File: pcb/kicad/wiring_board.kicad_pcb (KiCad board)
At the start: 2 copper layers, 47 x 72 mm, 13 parts, among them J1 2604-1106, J2 5V out (flex jumper)

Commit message: Boards for v0.4: ring board, mic carrier, riser, cover flex, EU cap board, wiring board posts
- Ring board, mic carrier and riser in pcb/sensor/ (D-50, D-60, D-68); carrier and riser fab
  packs; the ring board waits on the MSR-2's CN2 part and map
- Riser 14 x 12 mm, pins above and between the posts; cover flex with the run past the GND
  contact post and a jog from the pad section (D-79)
- EU cap board on the carrier, closed snap windows, wider with the face plate (D-56, D-70,
  D-77, D-78); EU 5 V board pins follow the back cover's pads
- Wiring board: WA-SMSI spacer posts in the 5 V area (SMT, spigot inside the board), J2
- ERC / DRC clean on every board
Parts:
- removed C1: 22uF 10V X5R, wiring_board:C_1206_3216Metric
- added P1: +5V post, wiring_board:Wurth_WA-SMSI_M2_SMT_Spacer_L7mm, F.Cu at (109.8, 116.5)
- added P2: GND post, wiring_board:Wurth_WA-SMSI_M2_SMT_Spacer_L7mm, F.Cu at (116.7, 116.5)
- J2: value 5V out (flex jumper) -> 5V out (FFC to the ring board)
- MH1, MH2, MH3, MH4: value MountingHole_2.6mm_NPTH -> MountingHole_3.2mm_M3_NPTH; footprint wiring_board:MountingHole_2.6mm_NPTH -> wiring_board:MountingHole_3.2mm_M3_NPTH
- moved J2 5.32 mm to (113.5, 124.8), turned to 90 degrees
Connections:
- J2 pad 2: GND -> +5V
- J2 pad 4: +5V -> GND
- J2 pad 6: +5V -> GND
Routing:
- net GND: track 15.1 -> 22.9 mm
- net +5V: track 15.6 -> 20.1 mm, vias 0 -> 2
- net /PE: vias 48 -> 46
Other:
- board text added: "2026-10-11"
- board text added: "P1 Wurth WA-SMSI M2 L7"
- board text added: "P2 Wurth WA-SMSI M2 L7"
- board text added: "wiring_board v0.4"
- board text removed: "2026-10-09"
- board text removed: "C1 22uF 10V X5R 1206"
- board text removed: "wiring_board v0.3"

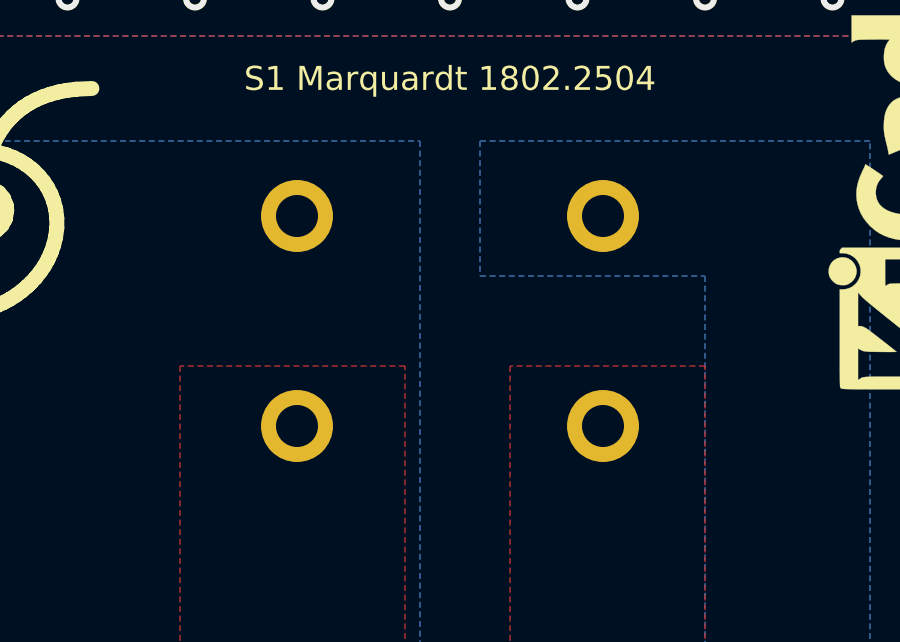
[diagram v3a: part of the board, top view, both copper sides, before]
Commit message: Mic on the boards, parts audit, rocker second source, CN2 land pattern, back cover fit (D-82..D-90)
- Prototype PCBWay packs for the ring board, EU cap board and cover flex; logos and URL on the
  boards with room for them
- CN2 mate: Molex 55909-2474 on an assumed 51338-2474 (D-82); land pattern from Molex
  SD-55909-003 rev J, B2B from SD-51338-003 rev K (D-89); contact map and pin 1 still open
- Microphone: Knowles SPK0641HT4H-1 + ADAU7002 on the ring board and the EU cap board, the mic
  carrier removed; face plate sound column on a gasket (D-83); C3 KEMET C1206C104J3GACTU C0G
  (D-85)
- Parts rule (active, stocked at DigiKey or Mouser) and audit: F1 3403.0166.11, cover flex 1 uF
  CL05A105KO5NNNC, rocker at Mouser 979-1802.2504 (D-84)
- Rocker: tabs soldered into plated slots accepted (D-86); E-Switch RA412C1100 second source,
  slotted footprint on the wiring board and the EU mains board, solder the rocker after the
  board is screwed down (D-88)
- Back cover: round-over 8.1 x 8.0 from the printed gauges (D-87); four tabs inside the long
  side walls into the housing's slots (D-90); back_gauges_PLA
- make stock / make order-push (pcb/tools/distributors.py): live DigiKey / Mouser stock and
  lifecycle, DigiKey myLists link and Mouser cart; keys from the environment only
- Boards ERC / DRC clean; make check, make eu, make check-renders pass; renders, fab and
  order packs regenerated
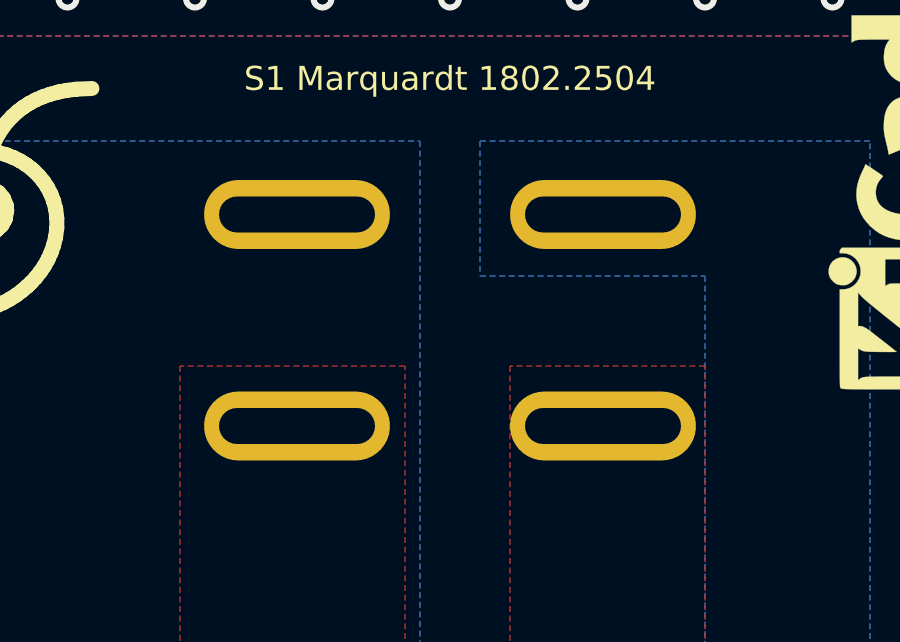
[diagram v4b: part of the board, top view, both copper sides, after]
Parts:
- S1: footprint wiring_board:Marquardt_1802.2504_DPST_PCB -> wiring_board:Rocker_DPST_Marquardt_1802.2504_E-Switch_RA412C1100

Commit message: v0.5: back cover ends, mains spacing 3.0 mm, NA fuse separation, labels, bare renders (D-101..D-106)
- D-101: back cover shell gauges (R15..R20.9); the stadium end is confirmed
- D-102: mains spacing 3.0 mm on high-CTI FR4 (MAINS_GAP, NA and EU)
- D-103: back cover end walls 1.40 mm, inside 0.2 mm longer (BC_END_WALL)
- D-104: NA wiring board: any two mains nets 3.0 mm apart, L_F re-routed
  F1.2 -> RV1.1, L_SW vias below F1, L_SW pour up towards the rocker;
  EU mains board checked, unchanged
- D-105: rocker silkscreen "E-Switch RA412C1100 or Marquardt 1802.2504",
  EU 5 V socket part on its label; bare 3D renders for every board
- D-106: version v0.5; v0.4 fab packs, PCBWay packs and renders removed
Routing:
- net /L_F: track 21.7 -> 18.6 mm
- net /L_SW: track 5.93 -> 4.75 mm
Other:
- board text added: "2026-10-12"
- board text added: "S1 E-Switch RA412C1100 or Marquardt 1802.2504"
- board text added: "wiring_board v0.5"
- board text removed: "2026-10-11"
- board text removed: "S1 Marquardt 1802.2504"
- board text removed: "wiring_board v0.4"
